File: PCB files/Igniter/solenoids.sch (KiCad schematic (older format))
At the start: 33 parts, among them J10 SL3, J11 SL4, J12 SL5, J8 SL1, J9 SL2, Q2 Q_NMOS_GDSD, Q3 Q_NMOS_GDSD, Q4 Q_NMOS_GDSD, Q5 Q_NMOS_GDSD, Q6 Q_NMOS_GDSD, U2 FDS8984, U3 FDS8984, U4 FDS8984

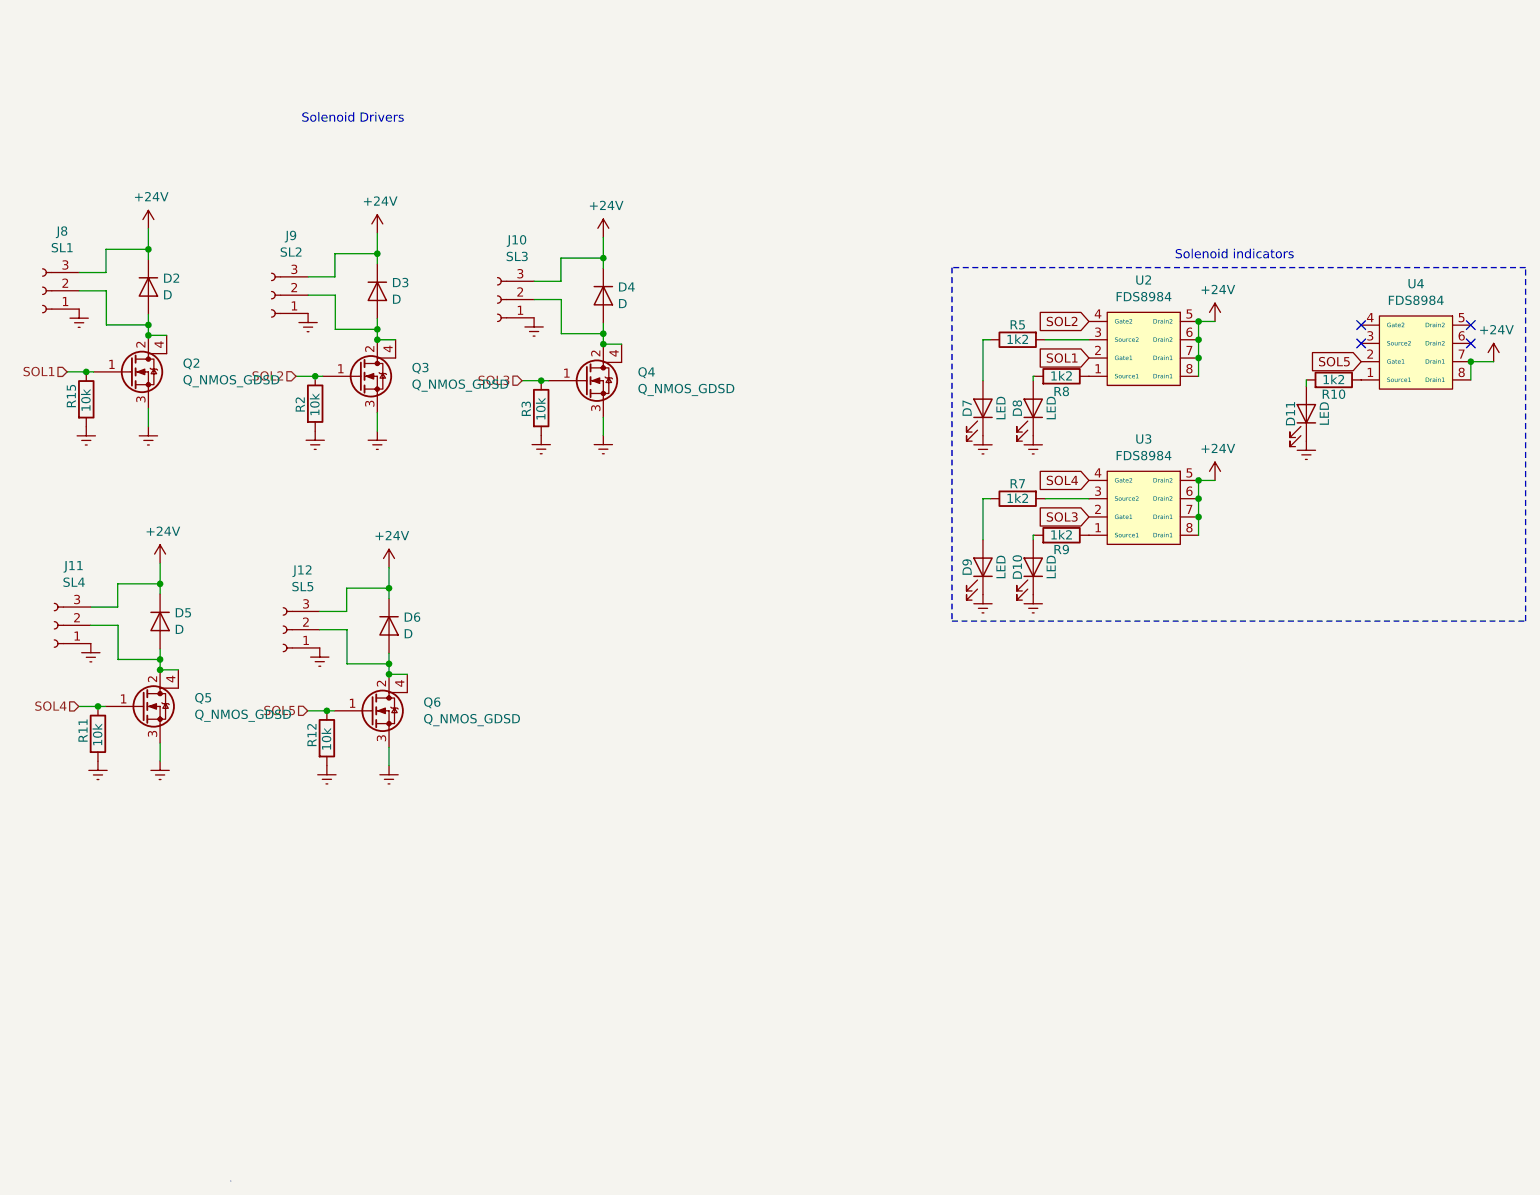
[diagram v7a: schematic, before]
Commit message: 1/15/2020
-Changed schematic grid to 10 mil and moved components onto grid
-Continued board routing
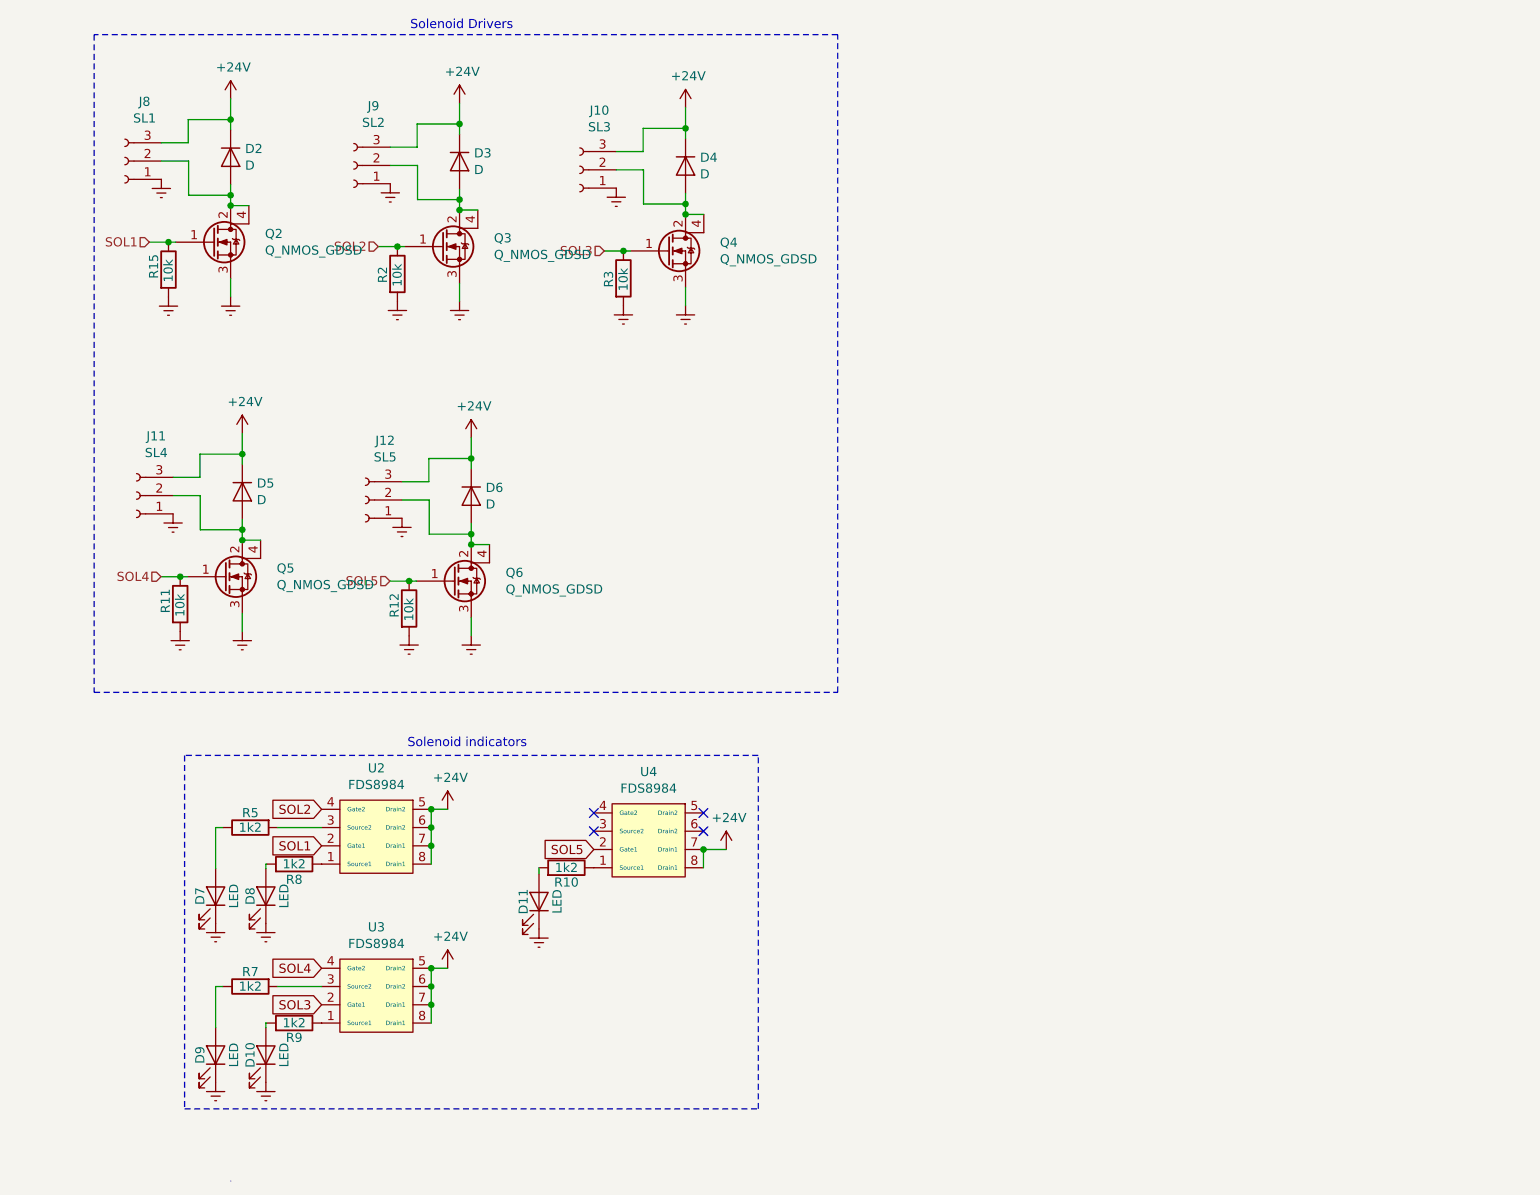
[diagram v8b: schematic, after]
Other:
- moved on the sheet: D10, D11, D2, D3, D4, D5, D6, D7, D8, D9, J10, J11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
